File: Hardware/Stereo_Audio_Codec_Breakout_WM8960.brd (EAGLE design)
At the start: 25.4 x 35.6 mm, 135 parts, among them J1 QWIIC, U4 WM8960, U5 LM1117, Y1 24 MHz

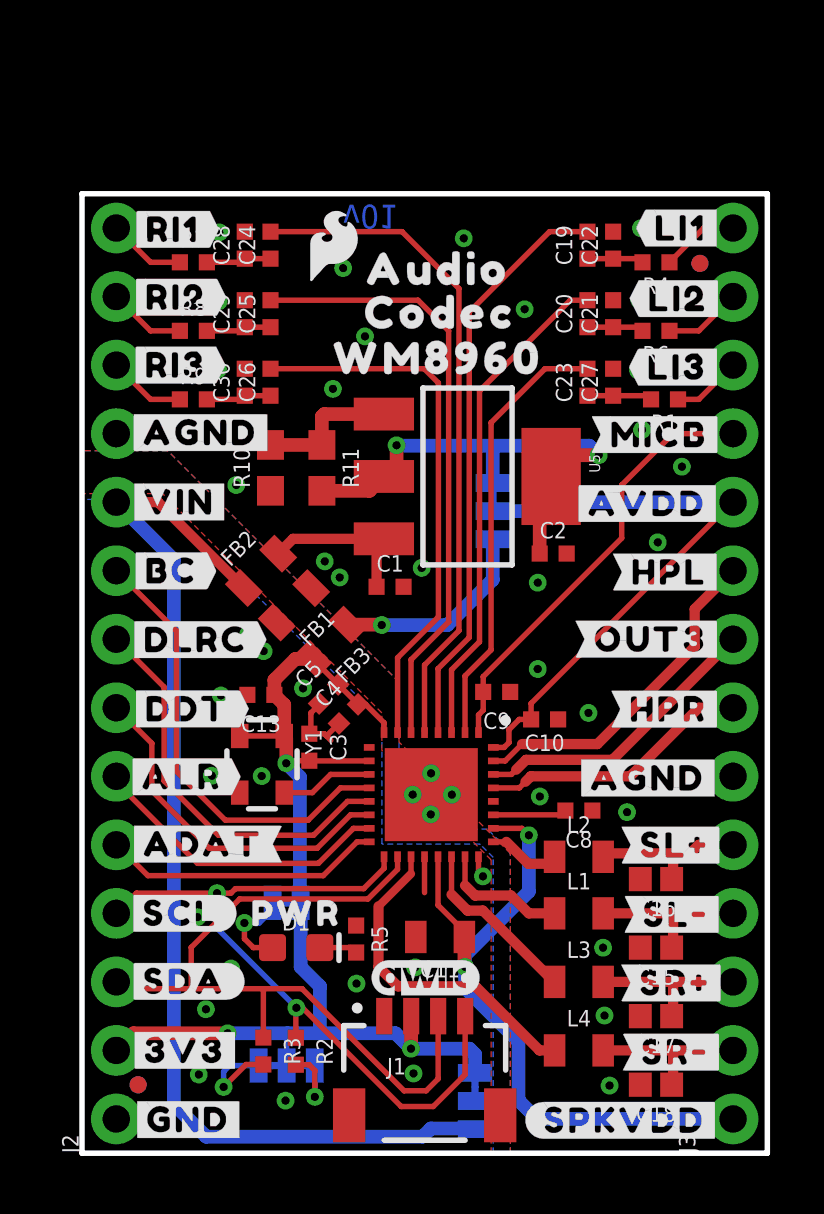
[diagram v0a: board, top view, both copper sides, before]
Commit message: Switched to single GND plane
-moved to smaller vreg for AVDD
-changed how power jumpers selection and isolation works
-created 3.3V and AVDD polygons on inner layers
-increased header length to allow for 100% analog pins to be on same side.
-split SPKVDD decoupling cap into two separate 4.7uF caps and put near IC pins
-added 10 ohm in series resistors on all data lines.
-moved input filtering passives closer to IC pins
-moved SPK filtering passive closer to IC pins
-updated all silk
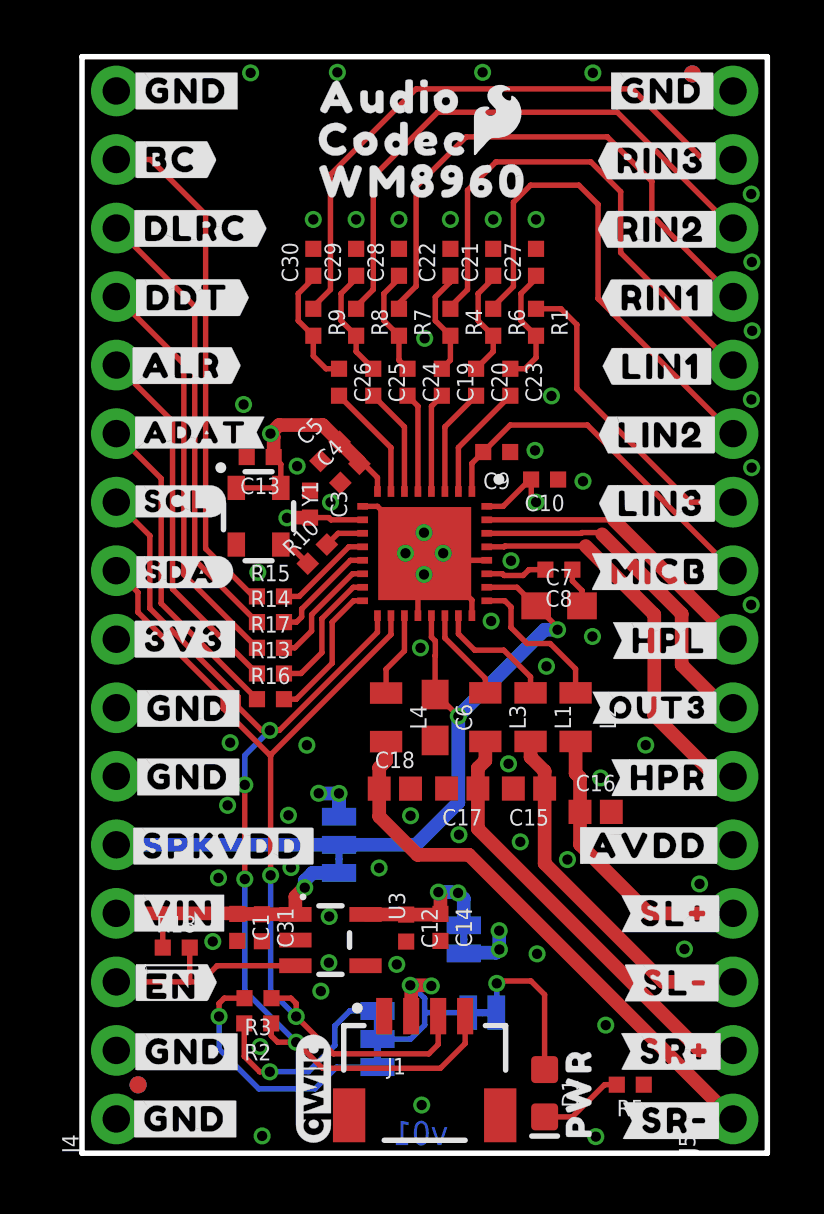
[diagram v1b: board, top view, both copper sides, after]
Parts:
- removed AVDD: (no value), SparkFun-Jumpers:SMT-JUMPER_3_1-NC_TRACE_SILK
- removed C11: 10uF, SparkFun-Capacitors:0805
- removed C2: 10uF, SparkFun-Capacitors:0402-TIGHT
- removed FB1, FB2, FB3: 600Ω, SparkFun-Coils:0805
- removed FRAME2: FRAME-LETTER, SparkFun-Aesthetics:CREATIVE_COMMONS
- removed J2, J3: (no value), SparkFun-Connectors:1X14_NO_SILK
- removed R11: 240, SparkFun-Resistors:0603
- removed U$23: (no value), output:#LI1#10
- removed U$24: (no value), output:#LI2#10
- removed U$25: (no value), output:#LI3#10
- removed U$42, U$43: (no value), output:#AGND#18
- removed U$5: (no value), output:#OUT3#8960896058
- removed U$87: (no value), output:#REG#50
- removed U$88: (no value), output:#VIN#52
- removed U5: LM1117, SparkFun-IC-Power:SOT223
- added AVDD-ISO: (no value), SparkFun-Jumpers:SMT-JUMPER_2_NC_TRACE_SILK
- added C12: 1.0uF, SparkFun-Capacitors:0402-TIGHT
- added C14, C31: 10uF, SparkFun-Capacitors:0402-TIGHT
- added C6, C7: 4.7uF, SparkFun-Capacitors:0603
- added FRAME1: FRAME-LEDGER, SparkFun-Aesthetics:CREATIVE_COMMONS
- added J4, J5: (no value), SparkFun-Connectors:1X16_NO_SILK
- added R13, R14, R15, R16, R17: 10Ω, SparkFun-Resistors:0402-TIGHT
- added R18: 100k, SparkFun-Resistors:0402-TIGHT
- added U$10: (no value), output:#AVDD#22
- added U$11, U$12, U$19, U$31, U$32, U$7, U$8, U$9: (no value), output:#GND#8
- added U$30: (no value), output:#SPKVDD#51
- added U$34: (no value), output:##EN##1
- added U$47: (no value), output:#RINPUT2#0
- added U$62: (no value), output:#LINPUT1#0
- added U3: XC6222B331MR-G, SparkFun-IC-Power:SOT23-5
- I2C: value JUMPER-SMT_3_2-NC_TRACE_NO-SILK -> JUMPER-SMT_3_2-NC_TRACE_SILK; device SparkFun-Jumpers:SMT-JUMPER_3_2-NC_TRACE_NO-SILK -> SparkFun-Jumpers:SMT-JUMPER_3_2-NC_TRACE_SILK
- LOGO1: value SFE_LOGO_NAME_FLAMEBLANK -> SFE_LOGO_NAME_FLAME.1_INCH; device SparkFun-Aesthetics:BLANK -> SparkFun-Aesthetics:SFE_LOGO_NAME_FLAME_.1
- R10: value 390 -> 10Ω; device SparkFun-Resistors:0603 -> SparkFun-Resistors:0402-TIGHT
- U$17: device output:#SPKVDD#13 -> output:#GND#8
- U$20: device output:#RI1#10 -> output:#AVDD#ISO#0
- U$21: device output:#RI2#10 -> output:#3V3#0
- U$22: device output:#RI3#10 -> output:#VIN#0
- U$38: device output:#3V3#17 -> output:##EN##2
- U$4: device SparkFun-Aesthetics:SFE_LOGO_FLAME_.1 -> output:#GND#8
- U$41: device output:#AGND#18 -> output:#OUT3#4
- U$44: device output:#AGND#18 -> output:#RINPUT1#0
- U$49: device output:#AVDD#22 -> output:#RINPUT3#0
- U$54: device output:#ADAT#26 -> output:#RIN3#0
- U$55: device output:#SCL#27 -> output:#ADAT#0
- U$56: device output:#SDA#28 -> output:#RIN2#0
- U$63: device output:AVDD32 -> output:#LINPUT2#0
- U$65: device output:#3V3#35 -> output:#LINPUT3#0
- U$66: device output:#RINPUT1#35 -> output:#SCL#0
- U$67: device output:#RINPUT2#35 -> output:#SDA#0
- U$68: device output:#RINPUT3#35 -> output:#RIN1#0
- U$76: device output:#LINPUT1#42 -> output:#LIN1#0
- U$77: device output:#LINPUT2#42 -> output:#LIN2#0
- U$78: device output:#LINPUT3#42 -> output:#LIN3#0
- moved LOGO1 46.1 mm to (12.5, 19.4), flipped to the bottom
- moved U$56 33.0 mm to (21.5, 34.2)
- moved U$54 30.5 mm to (21.5, 36.8)
- moved U$4 30.4 mm to (3.83, 3.77)
- moved U$20 27.0 mm to (9.60, 7.94), flipped to the bottom
- moved LOGO4 24.3 mm to (12.7, 30.2)
- moved U$21 20.9 mm to (12.1, 12.6), flipped to the bottom
- moved U$22 20.8 mm to (11.9, 10.2), flipped to the bottom
- moved U$17 20.6 mm to (3.94, 14.0), flipped to the bottom
- moved U$64 18.1 mm to (5.22, 11.4)
- moved U$55 17.8 mm to (4.22, 26.7)
- moved U$44 16.4 mm to (20.0, 31.7), flipped to the bottom
- moved U$68 16.1 mm to (21.5, 31.7), flipped to the top
- moved U$73 15.2 mm to (5.58, 26.7)
- moved U$45 15.2 mm to (3.60, 8.90)
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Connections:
- removed net AGND: C1.2, C10.1, C15.2, C16.2, C17.2, C18.2, C2.2, C21.2, C22.2, C27.2, C28.2, C29.2, C30.2, C8.1, C9.1, FB1.1, J2.11, J3.6, R10.1, U4.28, U4.PADDLE
- removed net DGND: C11.2, C13.2, C3.1, C4.1, C5.1, FB1.2, J1.1, J2.1, R5.1, U4.20, U4.24, U4.9, Y1.2
- removed net N$45: C1.1, FB2.2, U5.3
- new net EN: J4.3, R18.2, U3.3
- new net GND: C1.2, C10.1, C12.2, C13.2, C14.2, C15.2, C16.2, C17.2, C18.2, C21.2, C22.2, C27.2, C28.2, C29.2, C3.1, C30.2, C31.2, C4.1, C5.1, C6.2, C7.2, C8.1, C9.1, J1.1, J4.1, J4.16, J4.2, J4.6, J5.16, R5.1, U3.2, U4.20, U4.24, U4.28, U4.9, U4.PADDLE, Y1.2
- new net N$21: R14.2, U4.13
- new net N$22: R15.2, U4.12
- new net N$23: R16.2, U4.16
- new net N$24: R17.2, U4.14
- net 3.3V: now also J4.8, SPKVDD.1; no longer FB3.2, J2.2, SPKVDD.3
- net ADCDAT: now also J4.11, R16.1; no longer J2.5, U4.16
- net ADCLRC: now also J4.12, R13.1; no longer J2.6, U4.15
- net AVDD: now also AVDD-ISO.2, J5.5; no longer AVDD.2, J3.10
- net AVDD-REG: now also AVDD-ISO.1, C12.1, C14.1, U3.5; no longer AVDD.3, C2.1, R11.2, U5.2, U5.4
- net BCLK: now also J4.15, R15.1; no longer J2.9, U4.12
- net DACDAT: now also J4.13, R17.1; no longer J2.7, U4.14
- net DACLRC: now also J4.14, R14.1; no longer J2.8, U4.13
- net HP_L: now also J5.8; no longer J3.9
- net HP_R: now also J5.6; no longer J3.7
- net LINPUT1: now also J5.12; no longer J3.14
- net LINPUT2: now also J5.11; no longer J3.13
- net LINPUT3: now also J5.10; no longer J3.12
- net MICBIAS: now also J5.9; no longer J3.11
- net N$11: now also R10.1; no longer U4.11
- net N$2: now also R13.2, U4.15; no longer AVDD.1, FB3.1
- net N$25: now also U4.11; no longer R11.1, U5.1
- net OUT3: now also J5.7; no longer J3.8
- net RINPUT1: now also J5.13; no longer J2.14
- net RINPUT2: now also J5.14; no longer J2.13
- net RINPUT3: now also J5.15; no longer J2.12
- net SCL: now also J4.10; no longer J2.4
- net SDA: now also J4.9; no longer J2.3
- net SPKVDD: now also C6.1, C7.1, J4.5; no longer C11.1, J3.1
- net SPK_LN: now also J5.3; no longer J3.4
- net SPK_LP: now also J5.4; no longer J3.5
- net SPK_RN: now also J5.1; no longer J3.2
- net SPK_RP: now also J5.2; no longer J3.3
- net VIN: now also C1.1, C31.1, J4.4, R18.1, SPKVDD.3, U3.1; no longer FB2.1, J2.10, SPKVDD.1
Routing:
- net VIN: track 41.0 -> 10.7 mm, vias 0 -> 1
- net N$30: track 24.8 -> 3.71 mm
- net 3.3V: track 41.3 -> 21.1 mm, vias 3 -> 6
- net RINPUT3: track 2.88 -> 22.6 mm
- net N$9: track 22.5 -> 4.03 mm
- net RINPUT2: track 2.88 -> 21.3 mm
- net N$29: track 21.7 -> 3.71 mm
- net RINPUT1: track 2.88 -> 20.5 mm
- net AVDD: track 22.3 -> 5.05 mm, vias 0 -> 3
- net LINPUT1: track 2.88 -> 19.4 mm
- net N$8: track 20.0 -> 4.35 mm
- net LINPUT2: track 2.88 -> 18.5 mm
- net SPK_RN: track 6.11 -> 20.6 mm
- net N$12: track 18.5 -> 4.03 mm
- net AVDD-REG: track 18.7 -> 5.66 mm
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- added copper zone on layer 15, net 3.3V
- added copper zone on layer 15, net AVDD
- added copper zone on layer 1, net GND
- added copper zone on layer 16, net GND
- added copper zone on layer 2, net GND
- removed copper zone on layer 1, net AGND
- removed copper zone on layer 16, net AGND
- removed copper zone on layer 1, net DGND
- removed copper zone on layer 16, net DGND
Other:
- board size 25.4 x 35.6 mm -> 25.4 x 40.6 mm

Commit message: Removed top layer GND pour
routed GND connections to Vias
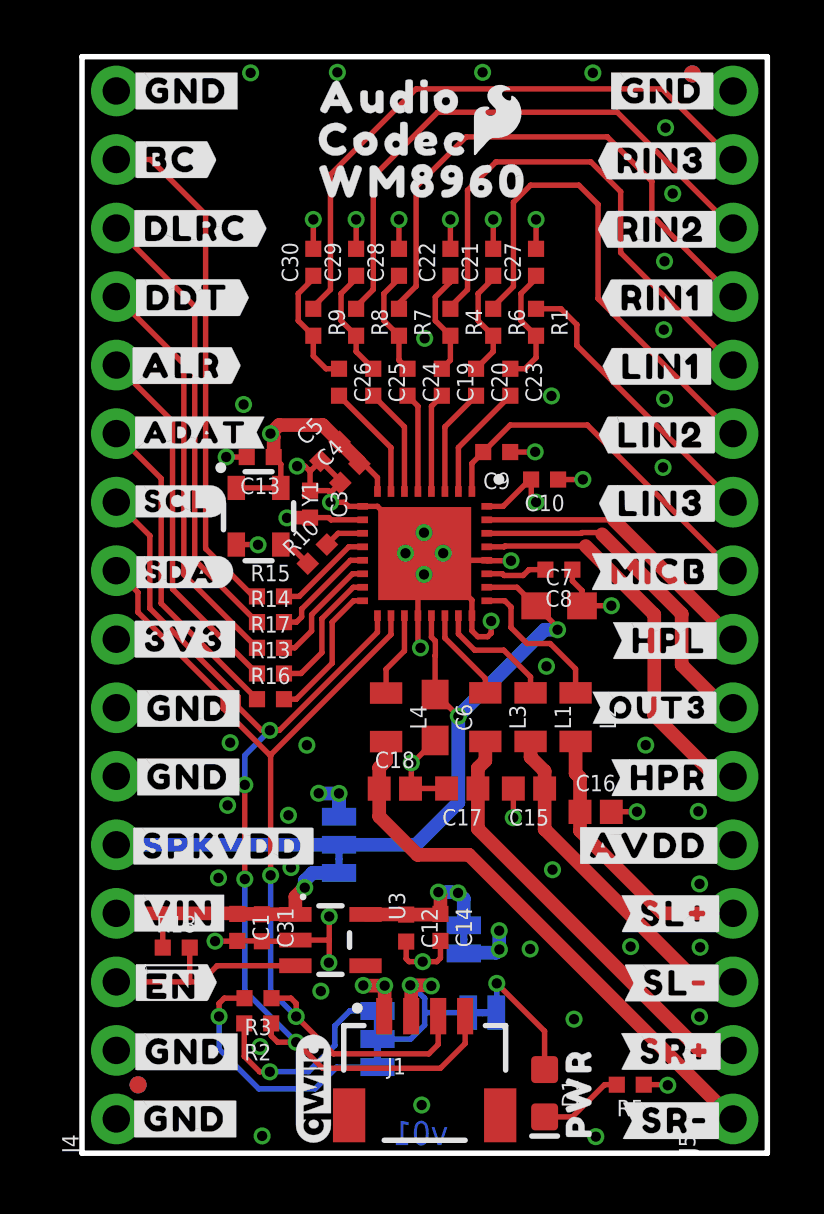
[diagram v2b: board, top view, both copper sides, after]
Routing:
- net GND: track 4.85 -> 43.5 mm, vias 60 -> 64
- net LINPUT3: track 11.7 -> 10.7 mm
- net N$7: track 5.89 -> 5.02 mm
- net SPK_LN: track 13.5 -> 12.8 mm
- removed copper zone on layer 1, net GND

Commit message: checklist catches - eng run
-Connected header pin (J4/7) to GND
-Added 4-layer board 1/2/3/4 in copper
-added ordering instructions
-added Selective solder path and moved some resistors to provide clearance on medium nozzle
-nudges some Vias to avoid cutting into silk
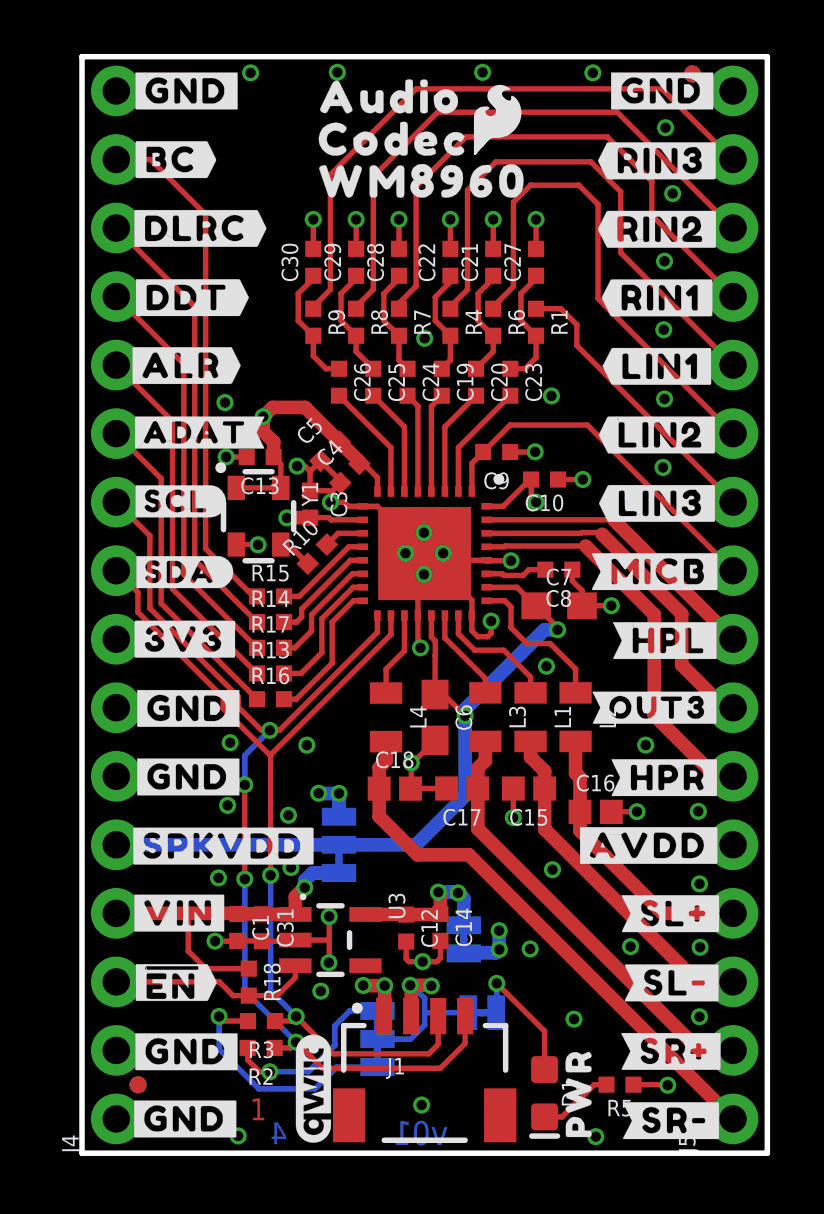
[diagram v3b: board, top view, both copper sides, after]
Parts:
- added LOGO5: SPECIAL_INSTRUCTIONS-ORDERING, SparkFun-Aesthetics:ORDERING_INSTRUCTIONS
- moved R18 2.98 mm to (6.18, 6.34), turned to 270 degrees
- moved R2 0.92 mm to (6.64, 3.90)
- moved R3 0.86 mm to (6.65, 4.90)
- moved R5 0.38 mm to (19.9, 2.54)
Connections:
- net GND: now also J4.7
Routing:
- net VIN: track 10.7 -> 13.4 mm
- net 3.3V: track 21.1 -> 22.4 mm
- net N$16: track 7.75 -> 6.80 mm
- net SDA: track 34.8 -> 34.2 mm
- net SCL: track 39.4 -> 38.8 mm
- net EN: track 8.16 -> 7.57 mm
- net GND: track 43.5 -> 43.9 mm, vias 64 -> 63
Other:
- board text added: "1"
- board text added: "2"
- board text added: "3"
- board text added: "4"
- board text added: "Board thickness is 1.6mm 4-Layer 1oz copper outer 0.5oz copper inner"

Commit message: Silk updates and codec package update
-corrected the I2S pins to be rounded flags (because they can be inputs or outputs)
-extended pads on codec FP to allow for better fillets. (also increased roundness of pads)
-corrected I2C address in schematic to 0x1A
-bumped version to v10
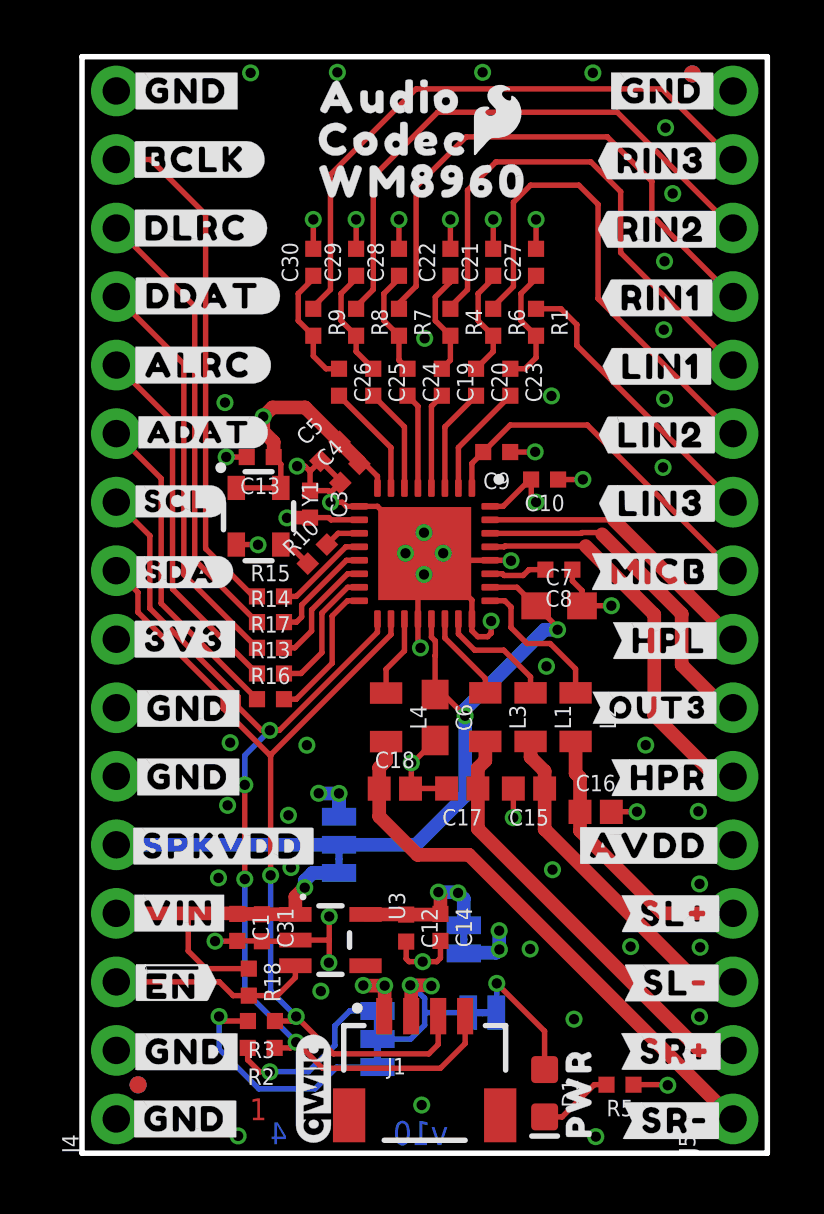
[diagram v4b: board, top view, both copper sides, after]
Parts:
- removed U$58: (no value), output:#DDT#30
- removed U$69: (no value), output:#BCLK#35
- removed U$70: (no value), output:#DACLRC#36
- removed U$71: (no value), output:#DACDAT#37
- removed U$72: (no value), output:#ADCLRC#38
- removed U$73: (no value), output:#ADCDAT#39
- added U$23: (no value), output:#ALRC#0
- added U$24: (no value), output:#DLRC#1
- added U$25: (no value), output:#DDAT#2
- added U$42: (no value), output:#ADAT#3
- added U$43: (no value), output:#ADCDAT#1
- added U$5: (no value), output:#BCLK#0
- U$52: device output:#BC#24 -> output:#ADCLRC#2
- U$53: device output:#DLRC#25 -> output:#DACDAT#3
- U$55: device output:#ADAT#0 -> output:#DACLRC#4
- U$57: device output:#ALR#29 -> output:#BCLK#5
- moved U$52 7.87 mm to (5.38, 29.2), flipped to the bottom
- moved U$57 7.68 mm to (4.27, 36.9), flipped to the bottom
- moved U$55 7.67 mm to (5.38, 34.3), flipped to the bottom
- moved U$53 2.86 mm to (5.61, 31.8), flipped to the bottom
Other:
- board text added: "v10"
- board text removed: "v01"
